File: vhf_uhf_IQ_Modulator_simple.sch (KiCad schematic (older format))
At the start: 78 parts

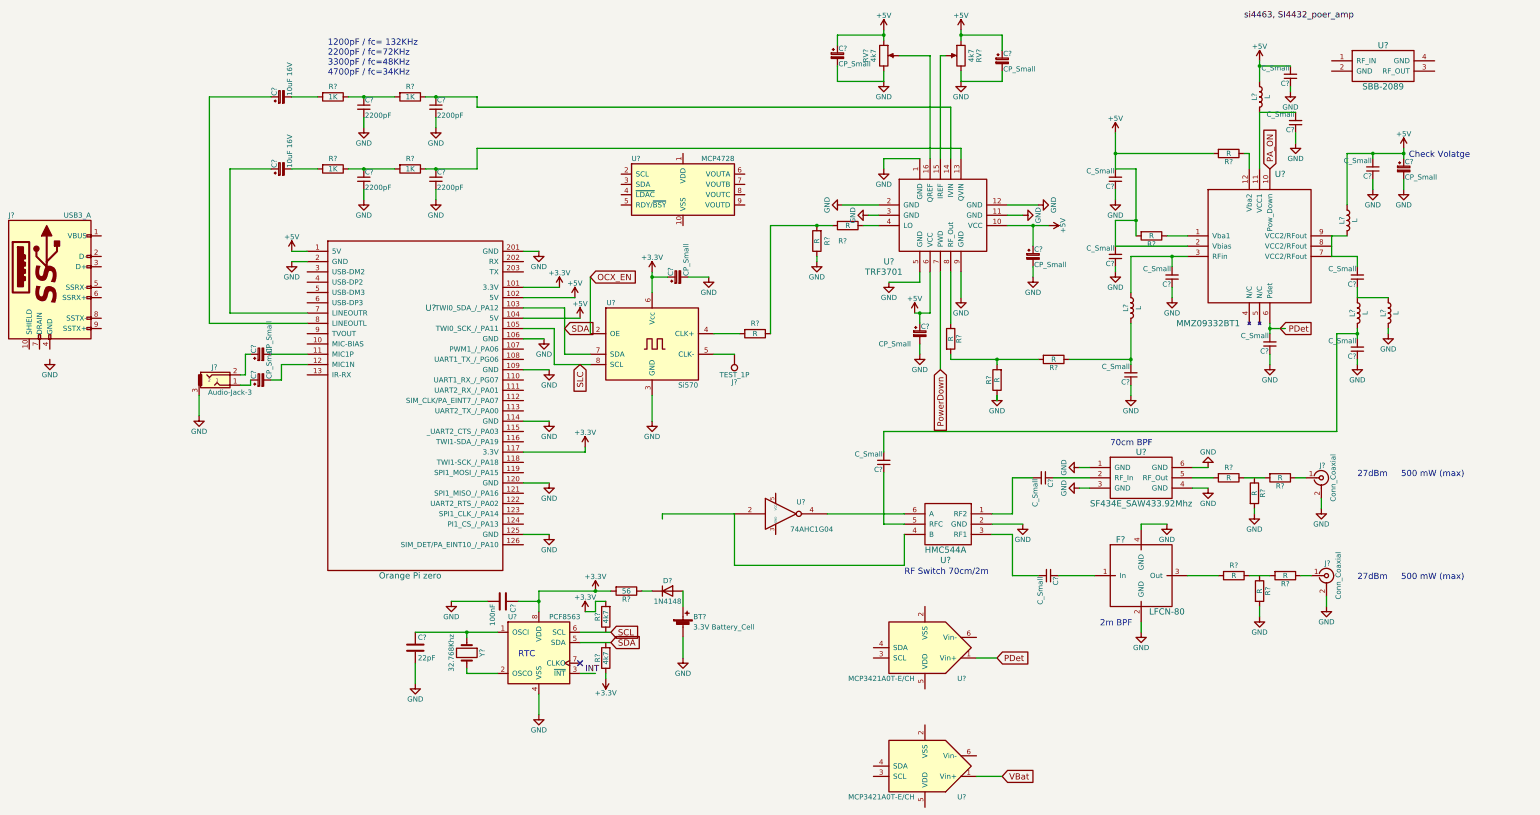
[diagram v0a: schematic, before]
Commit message: 2m filter and rf switch
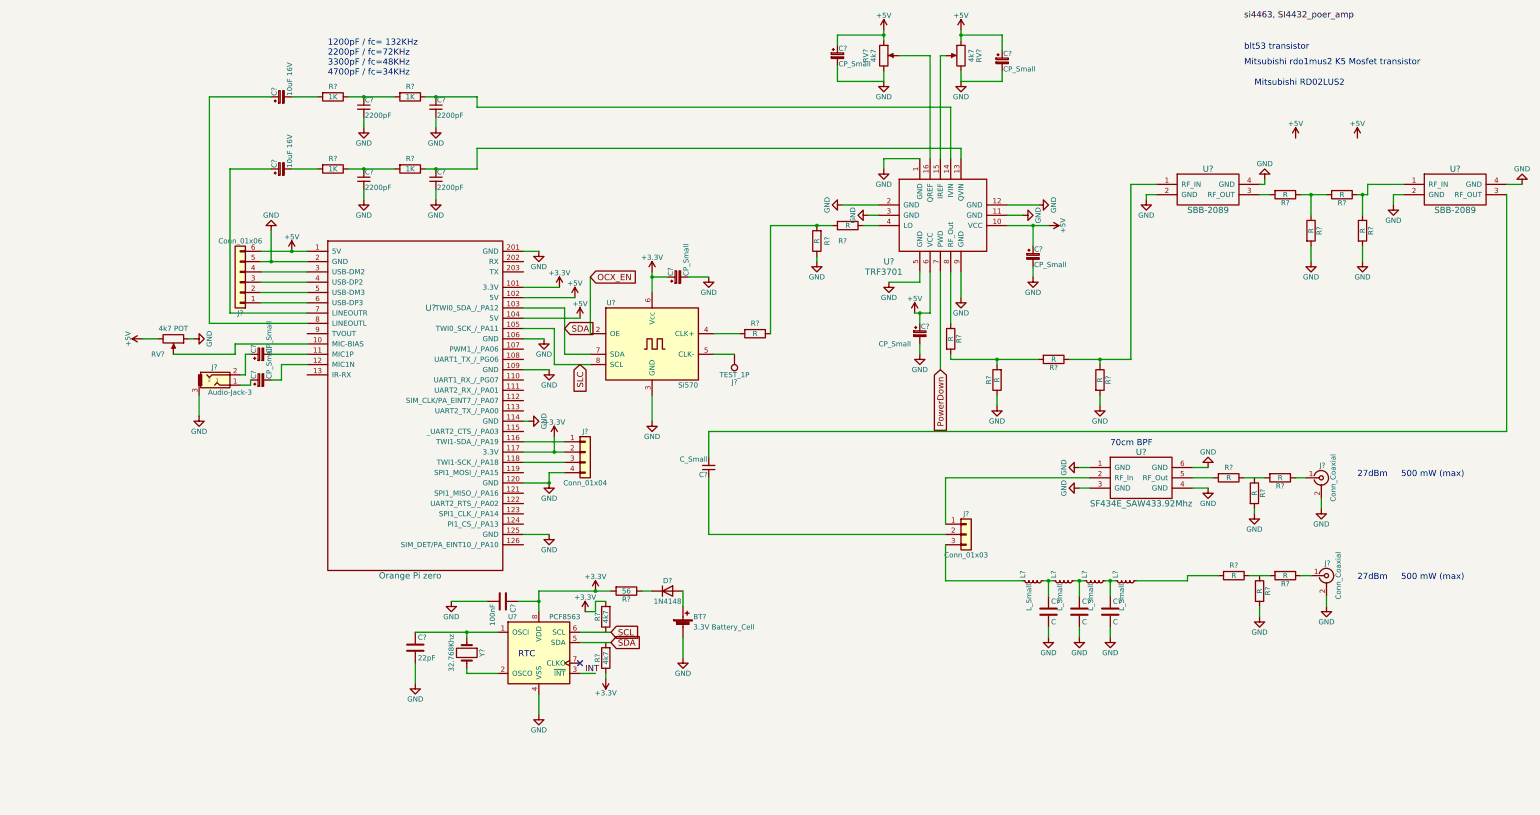
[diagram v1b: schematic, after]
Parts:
- removed C?: CP_Small, symbol CP_Small
- removed C? (x12): C_Small, symbol C_Small
- removed F?: LFCN-80, symbol LFCN-80
- removed J?: USB3_A, symbol USB3_A
- removed L? (x5): L, symbol L
- removed R? (x2): R, symbol R
- removed U?: SBB-2089, symbol SBB-2089
- removed U?: HMC544A, symbol HMC544A
- removed U?: 74AHC1G04, symbol 74AHC1G04
- removed U?: MMZ09332BT1, symbol MMZ09332BT1
- removed U? (x2): MCP3421A0T-E/CH, symbol MCP3421A0T-E/CH
- removed U?: MCP4728, Housings_SSOP:MSOP-10_3x3mm_Pitch0.5mm, symbol MCP4728
- added C? (x3): C, symbol C
- added J?: Conn_01x06, symbol Conn_01x06
- added J?: Conn_01x04, symbol Conn_01x04
- added J?: Conn_01x03, symbol Conn_01x03
- added L? (x4): L_Small, symbol L_Small
- added R? (x5): R, symbol R
- added RV?: 4k7 POT, symbol POT
- added U? (x2): SBB-2089, symbol SBB-2089
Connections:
- net +3V3: now also J?.2 (Pin_2)
- net +5V: now also J?.6 (Pin_6), RV?.3
- net GND: now also C?.2, C?.2, C?.2, J?.4 (Pin_4), J?.5 (Pin_5), R?.2, R?.2, R?.2, RV?.1, U?.2 (GND), U?.2 (GND), U?.4 (GND), U?.4 (GND)
- net at R?.2: now also L?.1
- net at R?.1: now also R?.1, U?.1 (RF_IN)
- net at U?.2 (RF_In): now also J?.1 (Pin_1)
- net at U?.10 (MIC-BIAS): now also RV?.2
- net at U?.116 (TWI1-SDA_/_PA19): now also J?.1 (Pin_1)
- net at U?.118 (TWI1-SCK_/_PA18): now also J?.3 (Pin_3)
- net at U?.3 (USB-DM2): now also J?.4 (Pin_4)
- net at U?.4 (USB-DP2): now also J?.3 (Pin_3)
- net at U?.5 (USB-DM3): now also J?.2 (Pin_2)
- net at U?.6 (USB-DP3): now also J?.1 (Pin_1)
- net at C?.1: now also J?.2 (Pin_2)
- net at C?.2: now also U?.3 (RF_OUT)
- new net: R?.2, U?.3 (RF_OUT)
- new net: R?.1, R?.1, U?.1 (RF_IN)
- new net: R?.1, R?.1, R?.2
- new net: C?.1, L?.1, L?.2 (x3)
- new net: J?.3 (Pin_3), L?.2
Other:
- note added: "Mitsubishi RD02LUS2"
- note added: "Mitsubishi rdo1mus2 K5 Mosfet transistor"
- note added: "blt53 transistor"
- note removed: "2m BPF"
- note removed: "Check Volatge"
- note removed: "RF Switch 70cm/2m"
- moved on the sheet: C?
